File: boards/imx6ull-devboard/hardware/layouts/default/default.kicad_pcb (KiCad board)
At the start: 2 copper layers, 90 parts

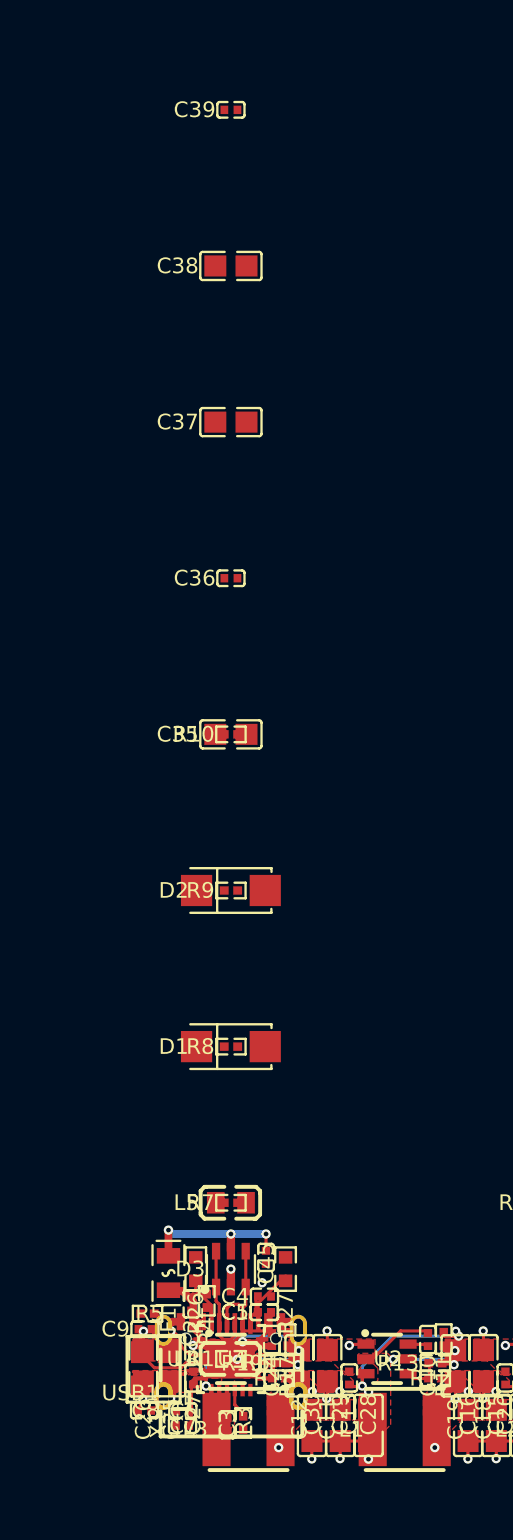
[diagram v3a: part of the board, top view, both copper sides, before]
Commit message: Audio + microSD subsystems v0
Audio: MAX98357A I²S Class-D 3W mono. nSD_MODE=VDD (stereo sum), GAIN=GND (+9dB),
ferrite + 1nF snubber on each output (commonized ferrite C1017). 3V3 VDD.

microSD: SOFNG TF-015 push-push slot, 4-bit SD mode, 3V3 signaling (no UHS-I),
direct 3V3 VDD (no power-cycle FET in v0). CMD 10kΩ + DAT[3:0] 47kΩ + CD 100kΩ
pull-ups per SD spec §3.2.

Both built clean. Atomic parts created via `ato create part`:
- Maxim_Integrated_MAX98357AETE_T (TQFN-16) from C910544
- SOFNG_TF_015 (microSD push-push) from C113206

Co-Authored-By: Claude Opus 4.7 (1M context) <noreply@anthropic.com>
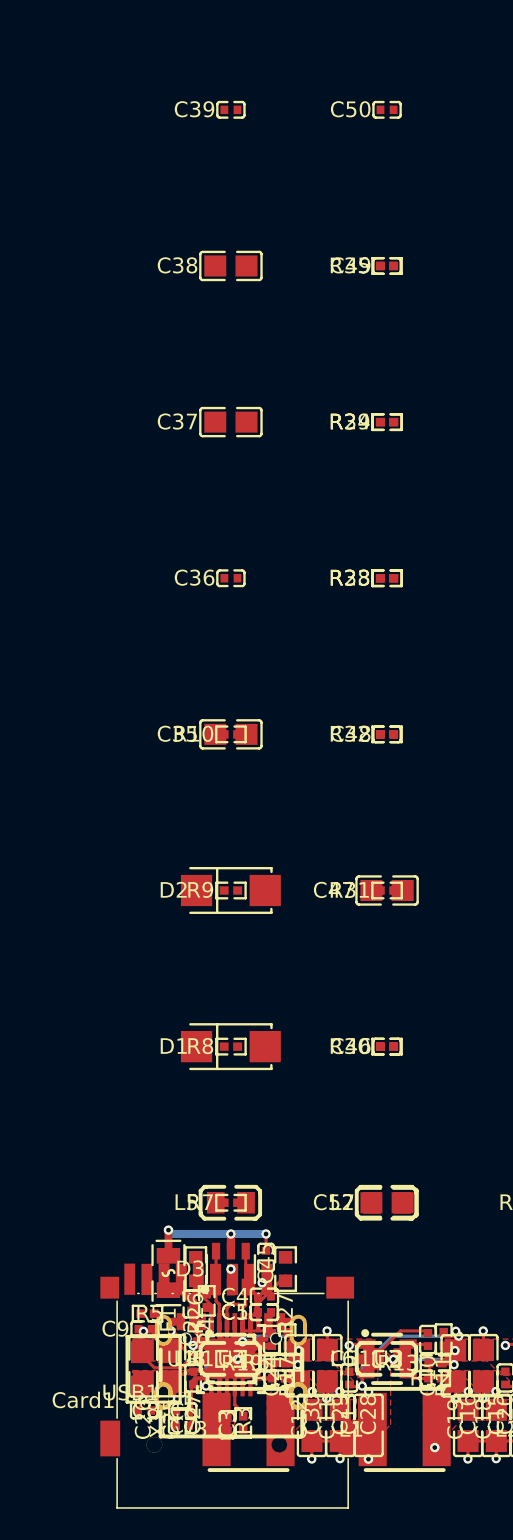
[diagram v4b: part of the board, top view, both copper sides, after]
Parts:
- added C46: 100nF ±10%, Samsung_Electro_Mechanics_CL05B104KO5NNNC:C0402, F.Cu at (10.0, -20.0)
- added C47: 10µF ±10%, Samsung_Electro_Mechanics_CL21A106KAYNNNE:C0805, F.Cu at (10.0, -30.0)
- added C48: 1µF ±10%, Samsung_Electro_Mechanics_CL05A105KA5NQNC:C0402, F.Cu at (10.0, -40.0)
- added C49: 1nF ±10%, YAGEO_CC0402KRX7R9BB102:C0402, F.Cu at (10.0, -70.0)
- added C50: 1nF ±10%, YAGEO_CC0402KRX7R9BB102:C0402, F.Cu at (10.0, -80.0)
- added C51: 100nF ±10%, Samsung_Electro_Mechanics_CL05B104KO5NNNC:C0402, F.Cu at (10.0, 0.00)
- added C52: 10µF ±10%, Samsung_Electro_Mechanics_CL21A106KAYNNNE:C0805, F.Cu at (10.0, -10.0)
- added Card1: , SOFNG_TF_015:TF-SMD_TF-015, F.Cu at (0.00, 0.00)
- added L6: L {ℝ+}H, Sunlord_GZ2012D601TF:L0805, F.Cu at (10.0, 0.00)
- added L7: L {ℝ+}H, Sunlord_GZ2012D601TF:L0805, F.Cu at (10.0, -10.0)
- added R28: 100kΩ ±1%, UNI_ROYAL_0402WGF1003TCE:R0402, F.Cu at (10.0, -50.0)
- added R29: 100kΩ ±1%, UNI_ROYAL_0402WGF1003TCE:R0402, F.Cu at (10.0, -60.0)
- added R30: 100kΩ ±1%, UNI_ROYAL_0402WGF1003TCE:R0402, F.Cu at (10.0, -20.0)
- added R31: 10kΩ ±1%, UNI_ROYAL_0402WGF1002TCE:R0402, F.Cu at (10.0, -30.0)
- added R32: 47kΩ ±1%, UNI_ROYAL_0402WGF4702TCE:R0402, F.Cu at (10.0, -40.0)
- added R33: 47kΩ ±1%, UNI_ROYAL_0402WGF4702TCE:R0402, F.Cu at (10.0, -50.0)
- added R34: 47kΩ ±1%, UNI_ROYAL_0402WGF4702TCE:R0402, F.Cu at (10.0, -60.0)
- added R35: 47kΩ ±1%, UNI_ROYAL_0402WGF4702TCE:R0402, F.Cu at (10.0, -70.0)
- added U8: , Maxim_Integrated_MAX98357AETE_T:TQFN-16_L3.0-W3.0-P0.50-BL-EP1.5, F.Cu at (0.00, 0.00)
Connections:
- C1 pad 1: power_3v3-hv -> hv
- C2 pad 1: power_3v3-hv -> hv
- C28 pad 1: power_3v3-hv -> hv
- C29 pad 1: power_3v3-hv -> hv
- C3 pad 1: power_3v3-hv -> hv
- C30 pad 1: power_3v3-hv -> hv
- C31 pad 1: power_3v3-hv -> hv
- C4 pad 1: power_3v3-hv -> hv
- C43 pad 1: hv -> cap_v3-power-hv
- C5 pad 1: power_3v3-hv -> hv
- L3 pad 2: power_3v3-hv -> hv
- R10 pad 2: power_3v3-hv -> hv
- R18 pad 1: power_3v3-hv -> hv
- R2 pad 2: power_3v3-hv -> hv
- R6 pad 2: power_3v3-hv -> hv
- R7 pad 2: power_3v3-hv -> hv
- R8 pad 2: power_3v3-hv -> hv
- R9 pad 2: power_3v3-hv -> hv
- U1 pad 1: power_3v3-hv -> hv
- U1 pad 19: power_3v3-hv -> hv
- U1 pad 9: power_3v3-hv -> hv
- U5 pad 4: power_3v3-hv -> hv
- U5 pad 6: power_3v3-hv -> hv
- U7 pad 8: hv -> cap_v3-power-hv
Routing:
- net SD: track 0.00 -> 56.2 mm, vias 0 -> 23
- net 2: track 56.2 -> 0.00 mm, vias 23 -> 0
- net cap_v3-power-hv: track 0.00 -> 5.89 mm, vias 0 -> 2
- net WS: track 0.00 -> 4.83 mm
- net 12: track 4.83 -> 0.00 mm
- net power_3v3-hv: track 3.86 -> 0.00 mm
- net hv: track 5.89 -> 3.86 mm, vias 2 -> 0

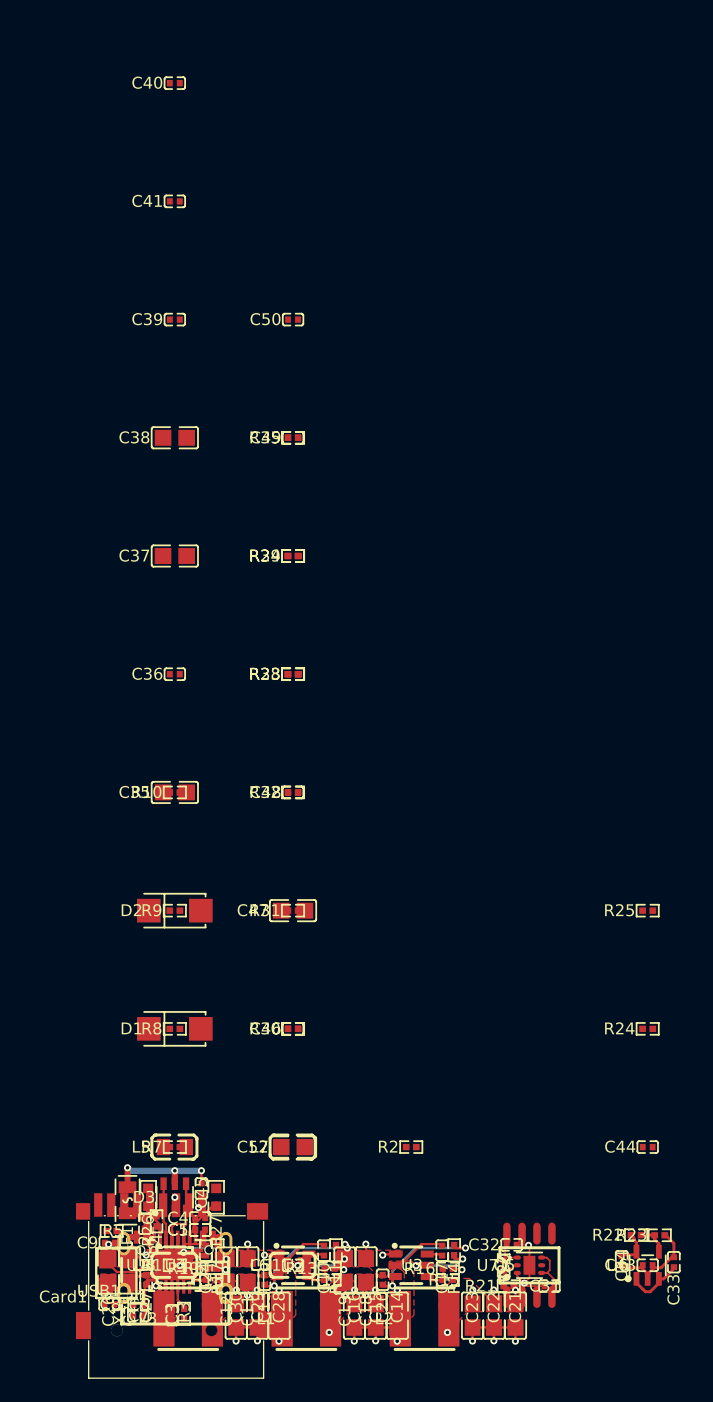
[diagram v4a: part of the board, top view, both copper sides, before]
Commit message: Power Input + reviewer fixes for USB-UART/Audio/microSD
Power Input subsystem v0:
  - USB-C #1 (built-in 5.1kΩ Rd + fuse + ESD) → SS54 ── 5V_BOARD
  - Bench DIBO terminal block → AO3401A rev-pol P-FET → SS54 ── 5V_BOARD
  - 100µF + 10µF + 100nF bulk on 5V_BOARD
  - Dropped HUSB238 for v0: connector's integrated Rd is sufficient for
    Vsafe5V from any USB-C source (sources advertise 1.5A/3A via Rp).
    Atomic part kept under src/parts/ for v2 swap-in if needed.

Batch reviewer fixes (USB-UART + Audio + microSD):
  - CRITICAL Audio nSD_MODE: was 100kΩ→VDD (= "Left only" with internal
    100kΩ pulldown forming a divider at 1.65V). Fixed to 1MΩ for SD≈0.30V
    in the Stereo (L+R)/2 sum band per datasheet table.
  - HIGH USB-UART VBUS backfeed: dropped buspower.hv tie to 5V_BOARD;
    only GND tied. CH340N runs from 5V_BOARD.
  - HIGH USB-UART/UART1 collides with i.MX boot ROM SDP: documented
    that MPU module must use UART2 not UART1 for console.
  - HIGH Audio output filter: ferrite + 1nF was an EMI snubber not Class-D
    filter. Switched to filterless mode (datasheet recommendation for
    <30cm cables); short twisted-pair speaker leads handle EMI.
  - HIGH microSD bulk cap: 10µF undersized for 200mA SD inrush. Bumped
    to 22µF X5R near slot.
  - FALSE POSITIVE on CH340N pinout (reviewer cited wrong datasheet —
    CH340DS1 covers CH340G/T not CH340N). Verified against actual WCH
    datasheet; auto-gen part is correct.

Build clean (27s), 45-line BOM. All five subsystems passing review.

Co-Authored-By: Claude Opus 4.7 (1M context) <noreply@anthropic.com>
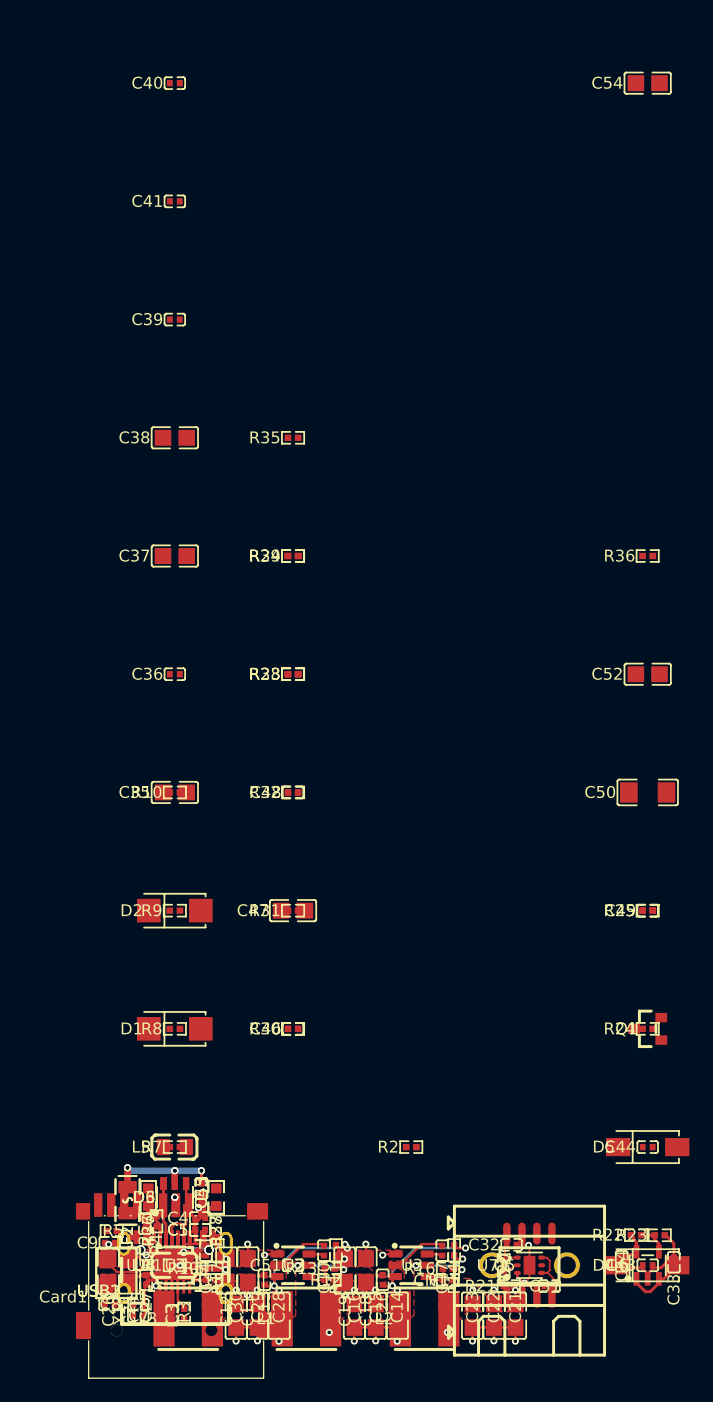
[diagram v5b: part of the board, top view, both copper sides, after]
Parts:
- removed L6, L7: L {ℝ+}H, Sunlord_GZ2012D601TF:L0805
- added C53: 100nF ±10%, Samsung_Electro_Mechanics_CL05B104KO5NNNC:C0402, F.Cu at (2.25, -6.50)
- added C54: 22µF ±20%, Samsung_Electro_Mechanics_CL21A226MAQNNNE:C0805, F.Cu at (40.0, -100.0)
- added CN1: , DIBO_DB910_6_35_2P_GN_S:CONN-TH_2P-P6.35_DB910-6.35-2P, F.Cu at (30.0, 0.00)
- added D4: Vf {ℝ+}V, MDD_Microdiode_Electronics_SS54:SMA_L4.4-W2.8-LS5.4-R-RD, F.Cu at (40.0, 0.00)
- added D5: Vf {ℝ+}V, MDD_Microdiode_Electronics_SS54:SMA_L4.4-W2.8-LS5.4-R-RD, F.Cu at (40.0, -10.0)
- added D6: , STMicroelectronics_USBLC6_2SC6:SOT-23-6_L2.9-W1.6-P0.95-LS2.8-BL, F.Cu at (0.00, -5.75)
- added F2: , BHFUSE_BSMD0805_050_15V:F0805, F.Cu at (-4.00, -5.50)
- added Q1: Vgs ℝ+V, Alpha___Omega_Semicon_AO3401A:SOT-23_L2.9-W1.3-P1.90-LS2.4-BR, F.Cu at (40.0, -20.0)
- added R36: 10kΩ ±1%, UNI_ROYAL_0402WGF1002TCE:R0402, F.Cu at (40.0, -60.0)
- added R37: 10kΩ ±1%, UNI_ROYAL_0603WAF1002T5E:R0603, F.Cu at (-2.25, -5.75)
- added R38: 10kΩ ±1%, UNI_ROYAL_0603WAF1002T5E:R0603, F.Cu at (3.50, -5.75)
- added USB2: , SHOU_HAN_TYPE_C_16PIN_2MD_073:USB-C-SMD_TYPE-C-6PIN-2MD-073, F.Cu at (0.00, 0.00)
- C49: value 1nF ±10% -> 100nF ±10%; footprint YAGEO_CC0402KRX7R9BB102:C0402 -> Samsung_Electro_Mechanics_CL05B104KO5NNNC:C0402
- C50: value 1nF ±10% -> 100µF ±20%; footprint YAGEO_CC0402KRX7R9BB102:C0402 -> Samsung_Electro_Mechanics_CL31A107MQHNNNE:C1206
- R29: value 100kΩ ±1% -> 1MΩ ±1%; footprint UNI_ROYAL_0402WGF1003TCE:R0402 -> UNI_ROYAL_0402WGF1004TCE:R0402
- moved C49 50.0 mm to (40.0, -30.0)
- moved C50 50.0 mm to (40.0, -40.0)
- moved C52 50.0 mm to (40.0, -50.0)
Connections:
- net anode renamed _ldo_snvs_out-anode
- net power_vbus-hv renamed connector-power_vbus-hv
- C11 pad 1: power_5v-hv -> cathode
- C12 pad 1: power_5v-hv -> cathode
- C13 pad 1: power_5v-hv -> cathode
- C18 pad 1: power_5v-hv -> cathode
- C19 pad 1: power_5v-hv -> cathode
- C20 pad 1: power_5v-hv -> cathode
- C25 pad 1: power_5v-hv -> cathode
- C26 pad 1: power_5v-hv -> cathode
- C27 pad 1: power_5v-hv -> cathode
- C33 pad 1: power_5v-hv -> cathode
- C37 pad 1: cathode -> power_snvs-cathode
- C44 pad 1: power_5v-hv -> cathode
- C45 pad 1: power_5v-hv -> decoupling_capacitor-power-hv
- C49 pad 1: snub_n-power-hv -> cathode
- C50 pad 1: snub_p-power-hv -> cathode
- C52 pad 1: hv -> cathode
- D1 pad 1: cathode -> power_snvs-cathode
- D2 pad 1: cathode -> power_snvs-cathode
- D3 pad 5: power_5v-hv -> decoupling_capacitor-power-hv
- F1 pad 2: power_5v-hv -> decoupling_capacitor-power-hv
- R11 pad 2: power_5v-hv -> cathode
- R14 pad 2: power_5v-hv -> cathode
- R17 pad 2: power_5v-hv -> cathode
- U2 pad 3: power_5v-hv -> cathode
- U3 pad 3: power_5v-hv -> cathode
- U4 pad 3: power_5v-hv -> cathode
- U6 pad 1: power_5v-hv -> cathode
- U6 pad 3: power_5v-hv -> cathode
- U7 pad 5: power_5v-hv -> cathode
- U8 pad 10: OUTN -> speaker_n_pad
- U8 pad 9: OUTP -> speaker_p_pad
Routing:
- net 0: track 92.7 -> 103.6 mm, vias 27 -> 30
- net lv: track 10.6 -> 21.2 mm
- net connector-cc[1]-10: track 0.00 -> 10.0 mm, vias 0 -> 3
- net usbc_pd-usb-DATA_N: track 0.00 -> 7.57 mm
- net usbc_pd-usb-DATA_P: track 0.00 -> 6.68 mm
